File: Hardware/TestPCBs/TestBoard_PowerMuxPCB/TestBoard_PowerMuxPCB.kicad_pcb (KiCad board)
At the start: 2 copper layers, 48 parts, among them J1 575-4, J2 575-4, J3 575-4, J4 575-4, J5 575-4, J6 53307-2471, J7 575-4, J8 Conn_01x03, J9 Conn_01x02

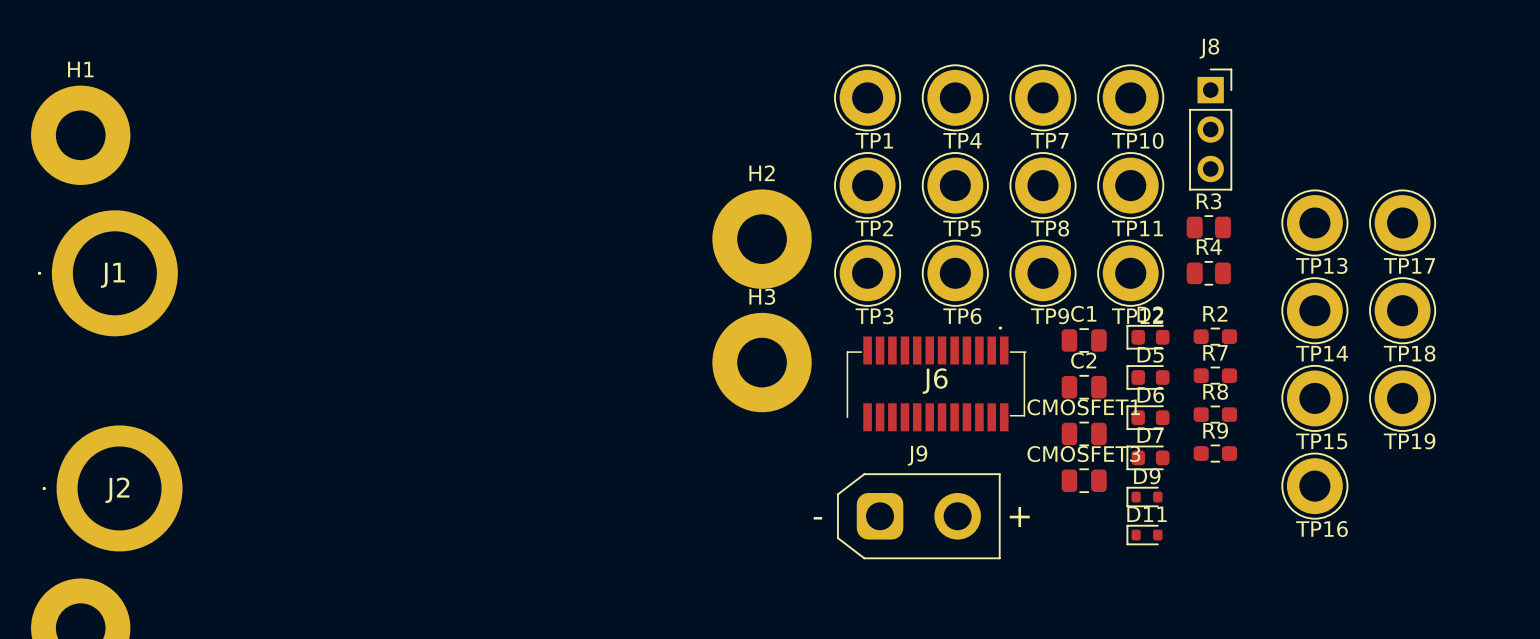
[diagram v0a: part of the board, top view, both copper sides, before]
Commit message: change testpoint footprint
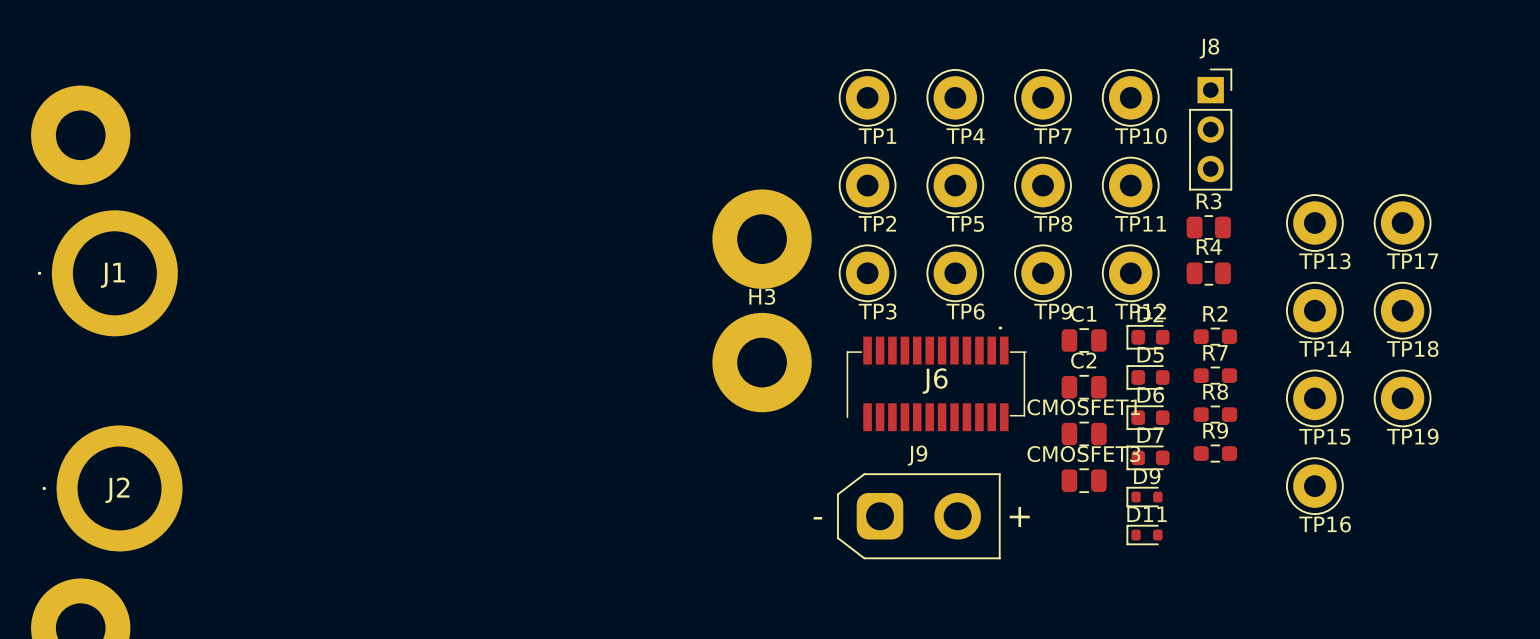
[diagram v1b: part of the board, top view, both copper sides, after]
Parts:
- TP1, TP10, TP11, TP12, TP13, TP14, TP15, TP16, TP17, TP18, TP19, TP2, TP3, TP4, TP5, TP6, TP7, TP8, TP9: footprint TestPoint:TestPoint_Loop_D3.80mm_Drill2.0mm -> TestPoint:TestPoint_Loop_D3.50mm_Drill1.4mm_Beaded

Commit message: test board mostly done
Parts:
- removed TP10, TP11, TP9: TestPoint, TestPoint:TestPoint_Loop_D3.50mm_Drill1.4mm_Beaded
- added D3: SMBJ15D-M3I, PowerBoardLib:P26_DO-214AA_SMB, F.Cu at (122.3, 121.9)
- added D4: SMBJ15D-M3I, PowerBoardLib:P26_DO-214AA_SMB, F.Cu at (123.3, 83.3)
- added Q1: SQJQ140E-T1_GE3, PowerBoardLib:TO200P800X182-5N, F.Cu at (129.3, 119.0)
- added Q2: SQJQ140E-T1_GE3, PowerBoardLib:TO200P800X182-5N, F.Cu at (129.2, 109.5)
- added Q3: SQJQ140E-T1_GE3, PowerBoardLib:TO200P800X182-5N, F.Cu at (129.3, 86.1)
- added Q4: SQJQ140E-T1_GE3, PowerBoardLib:TO200P800X182-5N, F.Cu at (129.3, 96.3)
- added R5: 1.5m, PowerBoardLib:RESC6432X89N, F.Cu at (121.0, 106.8)
- added R6: 1.5m, PowerBoardLib:RESC6432X89N, F.Cu at (121.1, 99.1)
- J6: footprint UTSVT_Connectors:533072471 -> PowerBoardLib:LVMux
- J8: footprint Connector_PinSocket_2.54mm:PinSocket_1x03_P2.54mm_Vertical -> Connector_PinHeader_2.54mm:PinHeader_1x03_P2.54mm_Vertical
- moved H1 164.9 mm to (182.5, 70.8)
- moved H3 144.8 mm to (182.5, 133.5)
- moved J1 137.0 mm to (128.5, 130.7)
- moved J8 129.4 mm to (170.5, 135.0), turned to -90 degrees
- moved TP1 128.8 mm to (176.8, 106.5)
- moved TP2 123.2 mm to (176.8, 102.2)
- moved TP3 118.2 mm to (176.8, 98.0)
- moved TP4 116.9 mm to (176.8, 93.8)
- moved TP12 113.1 mm to (182.5, 106.5)
- moved TP7 107.7 mm to (176.8, 85.2)
- moved TP8 107.0 mm to (176.8, 89.5)
- moved TP5 106.3 mm to (176.8, 76.5)
- moved D7 106.1 mm to (185.2, 102.2), turned to 90 degrees
- moved TP6 105.9 mm to (176.8, 81.0)
- moved H2 102.6 mm to (107.5, 133.5)
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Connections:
- J6 pad 7: /FTL1 -> /FTL2
- J9 pad 1: /Out -> GND
- J9 pad 2: GND -> /Out
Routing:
- net +3.3V: track 0.00 -> 75.1 mm
- net /V1: track 0.00 -> 48.0 mm
- net /Out: track 0.00 -> 46.8 mm
- net /SHDN: track 0.00 -> 44.1 mm, vias 0 -> 1
- net /V2: track 0.00 -> 42.2 mm
- net /CHL2: track 0.00 -> 40.7 mm
- net /GATE1: track 0.00 -> 38.2 mm, vias 0 -> 2
- net /VDL2: track 0.00 -> 36.3 mm
- net /DISABLE1: track 0.00 -> 35.8 mm
- net /GATE2: track 0.00 -> 34.0 mm, vias 0 -> 2
- net /FTL2: track 0.00 -> 33.3 mm
- net /FTL1: track 0.00 -> 32.9 mm
- net /VDL1: track 0.00 -> 30.0 mm
- net /CHL1: track 0.00 -> 29.3 mm
- net /DISABLE2: track 0.00 -> 28.8 mm
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- added copper zone on F.Cu, net /Out
- added copper zone on F.Cu, net /SENSE1
- added copper zone on F.Cu, net /SENSE2
- added copper zone on F.Cu, net /SOURCE1
- added copper zone on F.Cu, net /SOURCE2
- added copper zone on F.Cu, net /V1
- added copper zone on F.Cu, net /V2
- added copper zone on B.Cu, net GND
- added copper zone on F.Cu, net GND
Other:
- board outline added: 82.5 x 70.2 mm
- board text added: "3V3"
- board text added: "CH1"
- board text added: "DIS1"
- board text added: "FTL1"
- board text added: "GND"
- board text added: "OFF"
- board text added: "Out"
- board text added: "SHDN CTRL"
- board text added: "V1"
- board text added: "V2"
- board text added: "VDL1"

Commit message: test board jlc files
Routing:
- net /SOURCE2: track 23.3 -> 19.9 mm
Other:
- board text added: "Frank Li claims all damages and responsibilities"
- board text added: "LV Mux Testboard"

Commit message: most prod files
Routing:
- net GND: track 0.25 -> 0.18 mm, vias 42 -> 40
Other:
- board text added: "CHL2"
- board text added: "DIS2"
- board text added: "FLT2"
- board text added: "VLD2"
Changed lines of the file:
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@@
 		)
 	)
-	(gr_text "VDL1	"
-		(at 180.25 87.5 90)
+	(gr_text "FLT2"
+		(at 180.25 87 90)
 		(layer "F.SilkS")
 		(effects
@@
 		)
 	)
-	(gr_text "CH1"
-		(at 180.25 91.5 90)
+	(gr_text "DIS2"
+		(at 180.25 91.25 90)
 		(layer "F.SilkS")
 		(effects
@@
 		)
 	)
-	(gr_text "DIS1"
-		(at 180.25 79 90)
+	(gr_text "CHL2"
+		(at 180.25 78.5 90)
 		(layer "F.SilkS")
 		(effects
@@
 		)
 	)
-	(gr_text "FTL1"
-		(at 180.25 83.25 90)
+	(gr_text "VLD2"
+		(at 180.25 82.75 90)
 		(layer "F.SilkS")
 		(effects
@@
 	)
 	(segment
-		(start 154.35 98.775)
-		(end 154.4 98.825)
-		(width 0.5)
-		(layer "F.Cu")
-		(net 1)
-	)
-	(segment
 		(start 140.33 101.6)
 		(end 140.38 101.65)
@@
 	)
 	(via
-		(at 154.4 98.825)
-		(size 0.6)
-		(drill 0.3)
-		(layers "F.Cu" "B.Cu")
-		(net 1)
-	)
-	(via
 		(at 136.61 117.92)
-		(size 0.6)
-		(drill 0.3)
-		(layers "F.Cu" "B.Cu")
-		(net 1)
-	)
-	(via
-		(at 147.5 98.75)
 		(size 0.6)
 		(drill 0.3)
@@
 	)
 	(segment
+		(start 140.001 88.401)
+		(end 143.6 92)
+		(width 0.5)
+		(layer "F.Cu")
+		(net 6)
+	)
+	(segment
 		(start 147.174998 96.925002)
 		(end 147.15 96.95)
@@
 	)
 	(segment
-		(start 140.001 88.401)
-		(end 143.6 92)
+		(start 147.174998 96.25)
+		(end 147.174998 96.925002)
 		(width 0.5)
 		(layer "F.Cu")
@@
 	)
 	(segment
-		(start 147.174998 96.25)
-		(end 147.174998 96.925002)
-		(width 0.5)
-		(layer "F.Cu")
-		(net 6)
-	)
-	(segment
 		(start 132.3 89.7145)
 		(end 133.6135 88.401)
@@
 	)
 	(segment
+		(start 147.174998 96.25)
+		(end 147.25 96.174998)
+		(width 0.5)
+		(layer "B.Cu")
+		(net 6)
+	)
+	(segment
+		(start 147.25 95.55)
+		(end 143.7 92)
+		(width 0.5)
+		(layer "B.Cu")
+		(net 6)
+	)
+	(segment
+		(start 147.25 96.174998)
+		(end 147.25 95.55)
+		(width 0.5)
+		(layer "B.Cu")
+		(net 6)
+	)
+	(segment
 		(start 143.7 92)
 		(end 143.6 92)
 		(width 0.5)
 		(layer "B.Cu")
-		(net 6)
-	)
-	(segment
-		(start 147.174998 96.25)
-		(end 147.25 96.174998)
-		(width 0.5)
-		(layer "B.Cu")
-		(net 6)
-	)
-	(segment
-		(start 147.25 95.55)
-		(end 143.7 92)
-		(width 0.5)
-		(layer "B.Cu")
-		(net 6)
-	)
-	(segment
-		(start 147.25 96.174998)
-		(end 147.25 95.55)
-		(width 0.5)
-		(layer "B.Cu")

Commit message: lv mux test board
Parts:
- added J10: Conn_01x02, Connector_PinHeader_2.54mm:PinHeader_1x02_P2.54mm_Vertical, F.Cu at (119.7, 110.9)
- added J11: Conn_01x02, Connector_PinHeader_2.54mm:PinHeader_1x02_P2.54mm_Vertical, F.Cu at (116.8, 88.2)
- D3, D4: footprint PowerBoardLib:P26_DO-214AA_SMB -> LV Carrier Library:SMBJ15DM3
- J6: footprint PowerBoardLib:LVMux -> LV Carrier Library:LVMux
- Q1, Q2, Q3, Q4: footprint PowerBoardLib:TO200P800X182-5N -> LV Carrier Library:SQJQ140E-T1_GE3
- R5, R6: value 1.5m -> 1.3m
- moved TP14 6.86 mm to (110.0, 119.4)
- moved TP13 4.26 mm to (111.2, 86.3)
- turned CMOSFET1 to 90 degrees
- turned CMOSFET3 to 90 degrees
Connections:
- CMOSFET1 pad 1: /GATE1 -> /SOURCE1
- CMOSFET1 pad 2: /SOURCE1 -> /GATE1
- CMOSFET3 pad 1: /GATE2 -> /SOURCE2
- CMOSFET3 pad 2: /SOURCE2 -> /GATE2
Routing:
- net /GATE2: track 34.0 -> 42.6 mm
- net /SOURCE1: track 20.6 -> 28.3 mm
- net /SOURCE2: track 19.9 -> 25.8 mm
- net /GATE1: track 38.2 -> 42.4 mm
- net /V2: track 42.2 -> 46.4 mm
- net /V1: track 48.0 -> 50.4 mm
- net GND: vias 40 -> 42
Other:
- board text added: "Gate1"
- board text added: "Gate2"
- board text added: "Source1"
- board text added: "Source2"
